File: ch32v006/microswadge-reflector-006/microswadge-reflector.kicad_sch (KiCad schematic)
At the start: 25 parts, among them J1 USB_C_Receptacle_USB2.0, U1 CH32V006F8U6, Y1 24MHz

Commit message: Bump design
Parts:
- removed R10, R11, R12, R13, R14, R9: 120Ω, Resistor_SMD:R_0402_1005Metric, symbol Swadge_Parts:R_US
- added BT1: Battery_Cell, Battery:BatteryHolder_Keystone_3009_1x2450, symbol Device:Battery_Cell
- added D1, D2, D3, D4, D5, D6: LED_RAGB, symbol Device:LED_RAGB
- added R5: 12kΩ, Resistor_SMD:R_0402_1005Metric, symbol Swadge_Parts:R_US
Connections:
- net BVDD: now also R5.1; no longer U2.B1 (NTC), U2.B2 (INT)
- net GND: now also BT1.2 (-)
- net LV0: now also D3.2 (A), D4.2 (A)
- net LV1: now also D5.2 (A), D6.2 (A)
- net LV2: now also D1.2 (A), D2.2 (A)
- net T1C1: now also U1.11 (PC4/T1C1_/T1/MCO/A2), D1.1 (RK), D3.1 (RK), D5.1 (RK)
- net T1C2: now also U1.12 (PC5/T1C2_/T1/T2/TX_/SCK), D1.3 (GK), D3.3 (GK), D5.3 (GK)
- net T1C3: now also U1.13 (PC6/T1C3_/T1/RX_/MOSI), D1.4 (BK), D3.4 (BK), D5.4 (BK)
- net T2C1: now also U1.7 (PC0/T1C1N_/T1/T2/TX_/MOSI_), D2.3 (GK), D4.3 (GK), D6.3 (GK)
- net T2C3: now also U1.10 (PC3/T1/T2), D2.1 (RK), D4.1 (RK), D6.1 (RK)
- net T2C4: now also U1.20 (PD6/T2/RX/TX_/MOSI_/A6), D2.4 (BK), D4.4 (BK), D6.4 (BK)
- net at C6.1, U2.A3 (BAT): now also BT1.1 (+)
- new net VNTC: R5.2, U2.B1 (NTC), U2.B2 (INT)

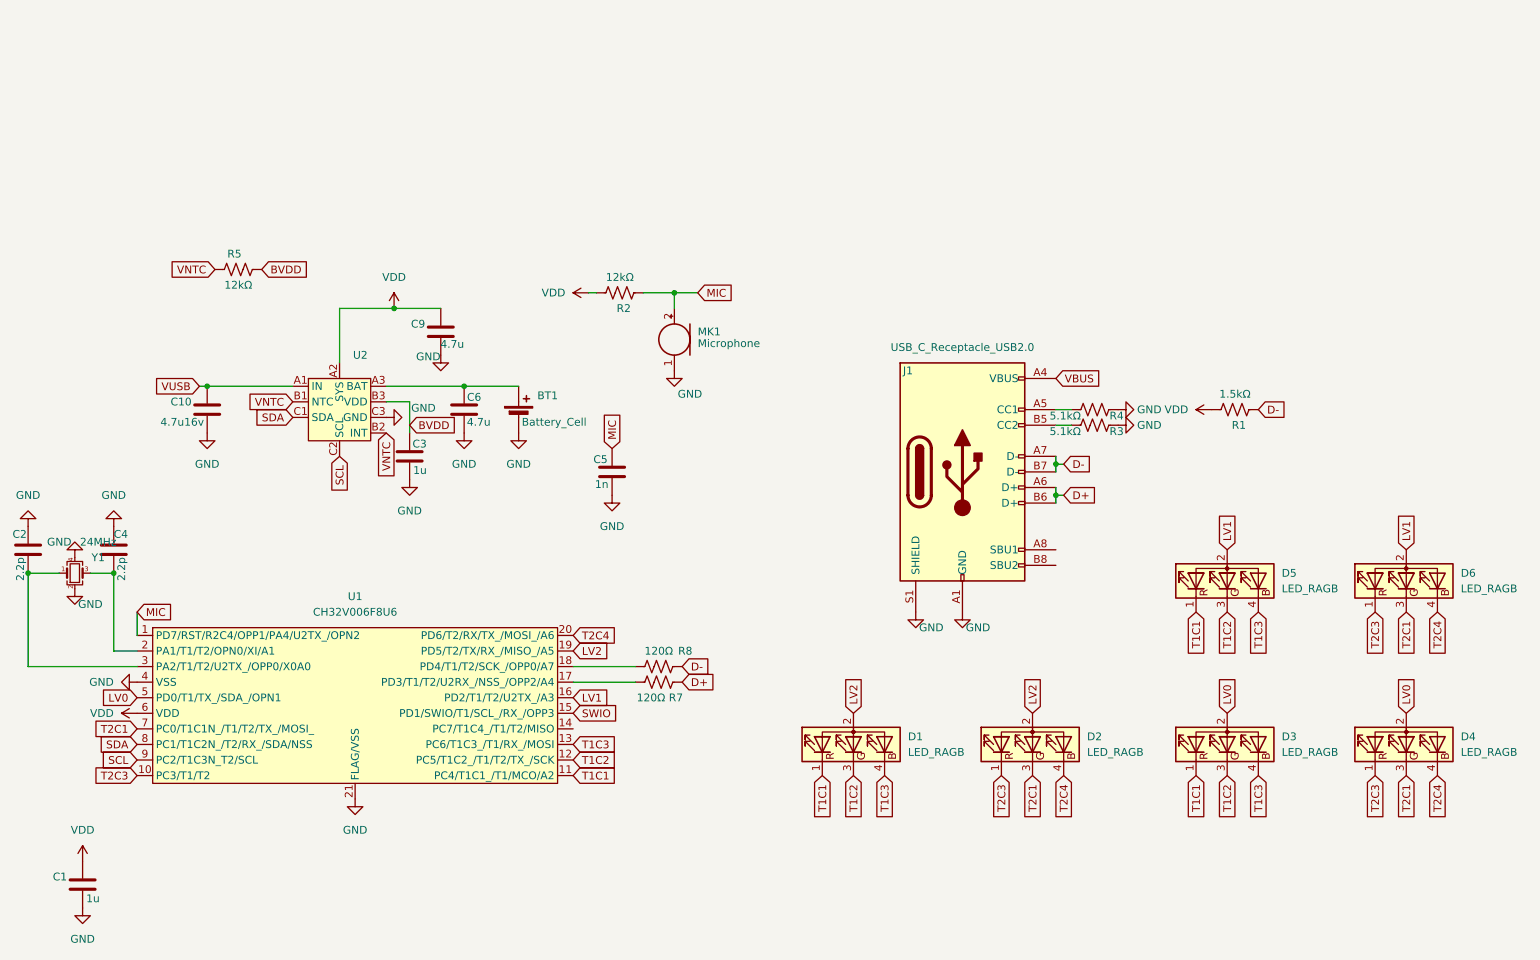
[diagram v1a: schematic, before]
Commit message: Bump microswadge reflector.
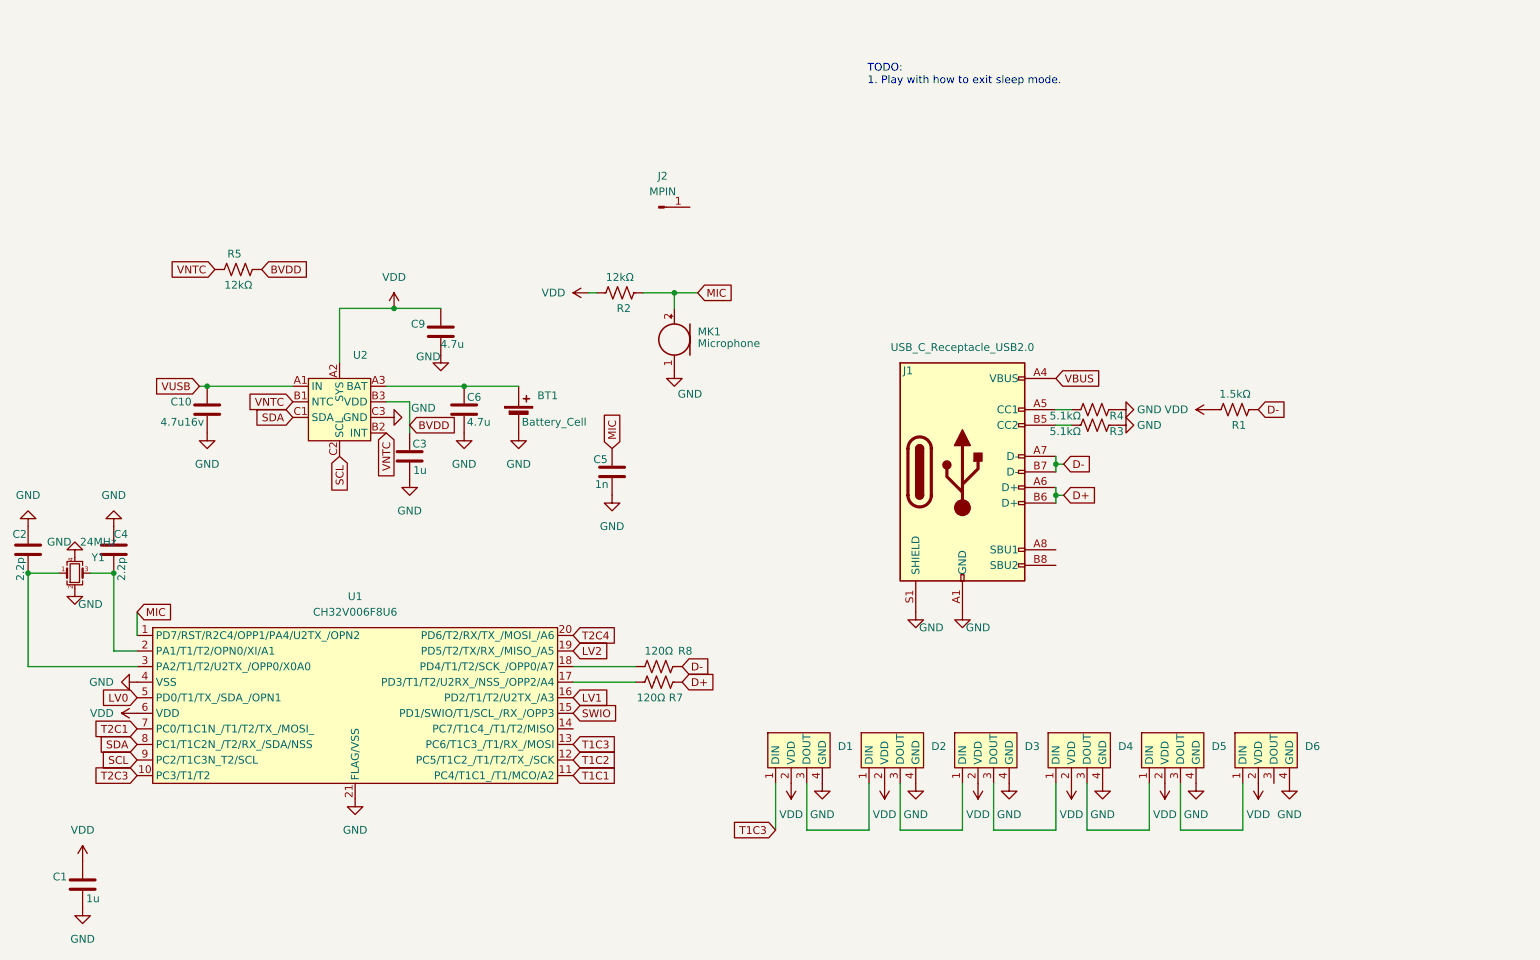
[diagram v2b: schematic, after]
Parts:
- removed D1, D2, D3, D4, D5, D6: LED_RAGB, symbol Device:LED_RAGB
- added D1, D2, D3, D4, D5, D6: ~, cnhardware:LC8812-SIDE-4020, symbol cnhardware:LC8812-SIDE-4020
- added J2: MPIN, TestPoint:TestPoint_Pad_D4.0mm, symbol Connector:Conn_01x01_Pin
- BT1: footprint Battery:BatteryHolder_Keystone_3009_1x2450 -> cnhardware:CR2450-TWOPAD; LCSC (none) -> C964809
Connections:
- net GND: now also D1.4 (GND), D2.4 (GND), D3.4 (GND), D4.4 (GND), D5.4 (GND), D6.4 (GND)
- net T1C3: now also D1.1 (DIN)
- net VDD: now also D1.2 (VDD), D2.2 (VDD), D3.2 (VDD), D4.2 (VDD), D5.2 (VDD), D6.2 (VDD)
- new net: D3.3 (DOUT), D4.1 (DIN)
- new net: D4.3 (DOUT), D5.1 (DIN)
- new net: D2.3 (DOUT), D3.1 (DIN)
- new net: D1.3 (DOUT), D2.1 (DIN)
- new net: D5.3 (DOUT), D6.1 (DIN)
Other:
- note added: "TODO: 1. Play with how to exit sleep mode."

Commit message: Bump updates
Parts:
- added J3: PGM, Connector_PinHeader_2.54mm:PinHeader_1x03_P2.54mm_Vertical, symbol Connector_Generic:Conn_01x03
- added U3: SC7A20, Package_LGA:LGA-12_2x2mm_P0.5mm, symbol Sensor_Motion:SC7A20
- D1, D2, D3, D4, D5, D6: LCSC (none) -> C5378721
- U2: value ~ -> AW32001ECSR
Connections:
- net T1C2 is gone; now on net GND: U1.12 (PC5/T1C2_/T1/T2/TX_/SCK)
- net GND: now also J3.1 (Pin_1), U3.1 (SDO), U3.8 (GNDIO), U3.9 (GND)
- net SCL: now also U3.12 (SCx)
- net SDA: now also U3.2 (SDx)
- net SWIO: now also J3.3 (Pin_3)
- net VDD: now also J3.2 (Pin_2), U3.10 (~{CS}), U3.3 (VDDIO), U3.7 (VDD)
- net VNTC: now also U3.5 (INT1)

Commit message: Update based on comments from fab
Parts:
- R2, R5: LCSC C22790 -> C25752
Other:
- note added: "Alternate: C2909060"
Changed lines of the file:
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@@
 		)
 	)
+	(text "Alternate: C2909060"
+		(exclude_from_sim no)
+		(at 185.674 135.382 0)
+		(effects
+			(font
+				(size 1.27 1.27)
+			)
+		)
+	)
 	(text "TODO:\n1. Play with how to exit sleep mode."
 		(exclude_from_sim no)
@@
 			)
 		)
-		(property "LCSC" "C22790"
+		(property "LCSC" "C25752"
 			(at 115.57 68.58 0)
 			(effects
@@
 			)
 		)
-		(property "LCSC" "C22790"
+		(property "LCSC" "C25752"
 			(at 53.34 64.77 0)
 			(effects
